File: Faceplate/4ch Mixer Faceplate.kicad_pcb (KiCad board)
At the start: 2 copper layers, 30.5 x 128.5 mm, 15 parts

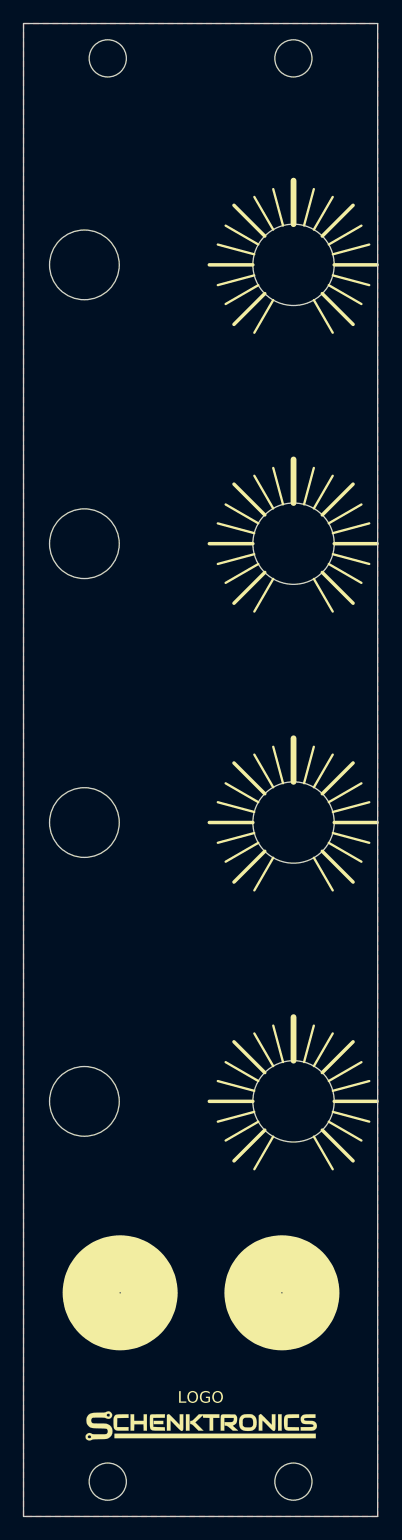
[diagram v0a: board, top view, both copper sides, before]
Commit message: Match mounting hole positions to the Attenuverter faceplate
Holes at 7.5 mm and 22.75 mm from the panel's left edge and 3 mm from the top
and bottom, as on the Attenuverter. DRC: no errors.
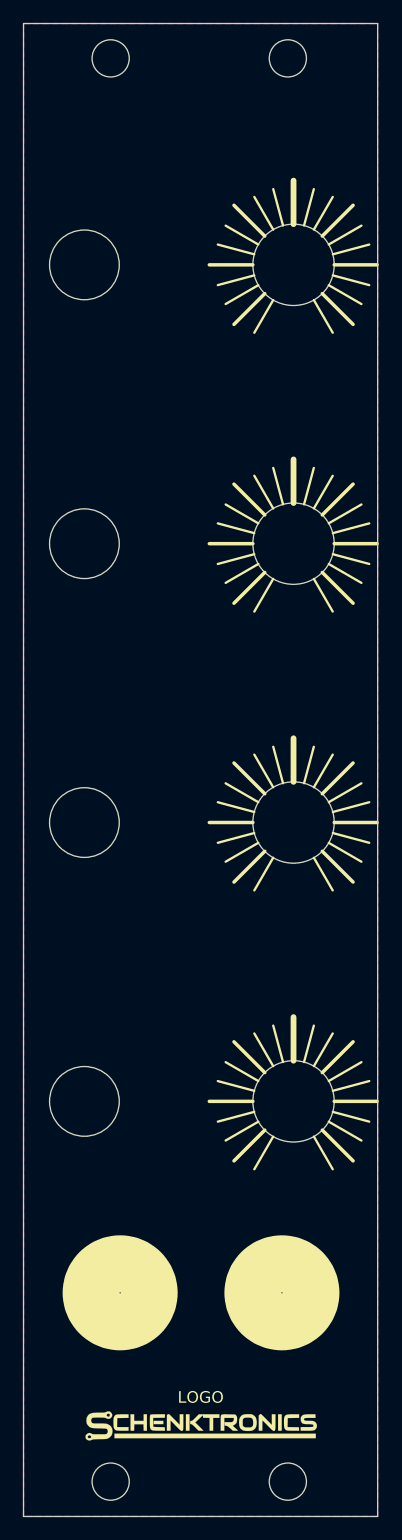
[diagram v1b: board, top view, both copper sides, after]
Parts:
- moved H2 0.48 mm to (122.5, 38.8)
- moved H4 0.48 mm to (122.5, 161.2)
- moved H1 0.25 mm to (107.3, 38.8)
- moved H3 0.25 mm to (107.3, 161.2)
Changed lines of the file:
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@@
 	(footprint "Panel:MountingHole_3.2mm"
 		(layer "F.Cu")
-		(at 107.01 38.75)
+		(at 107.26 38.75)
 		(attr board_only exclude_from_pos_files exclude_from_bom)
 		(property "Reference" "H1"
@@
 	(footprint "Panel:MountingHole_3.2mm"
 		(layer "F.Cu")
-		(at 122.99 38.75)
+		(at 122.51 38.75)
 		(attr board_only exclude_from_pos_files exclude_from_bom)
 		(property "Reference" "H2"
@@
 	(footprint "Panel:MountingHole_3.2mm"
 		(layer "F.Cu")
-		(at 107.01 161.25)
+		(at 107.26 161.25)
 		(attr board_only exclude_from_pos_files exclude_from_bom)
 		(property "Reference" "H3"
@@
 	(footprint "Panel:MountingHole_3.2mm"
 		(layer "F.Cu")
-		(at 122.99 161.25)
+		(at 122.51 161.25)
 		(attr board_only exclude_from_pos_files exclude_from_bom)
 		(property "Reference" "H4"
